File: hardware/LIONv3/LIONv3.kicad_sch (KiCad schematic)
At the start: 31 parts, among them SW1 RESET, SW2 BOOT, U14 HC-1_25-2PWT, U15 HC-1_25-2PWT, U19 HC-1_25-2PWT, U2 TYPE-C_16PIN_2MD(073), U21 USBLC6-2SC6, U3 ESP32-C6-MINI-1-N4, U4 TMP112AIDRLR, U9 HC-1_25-2PWT

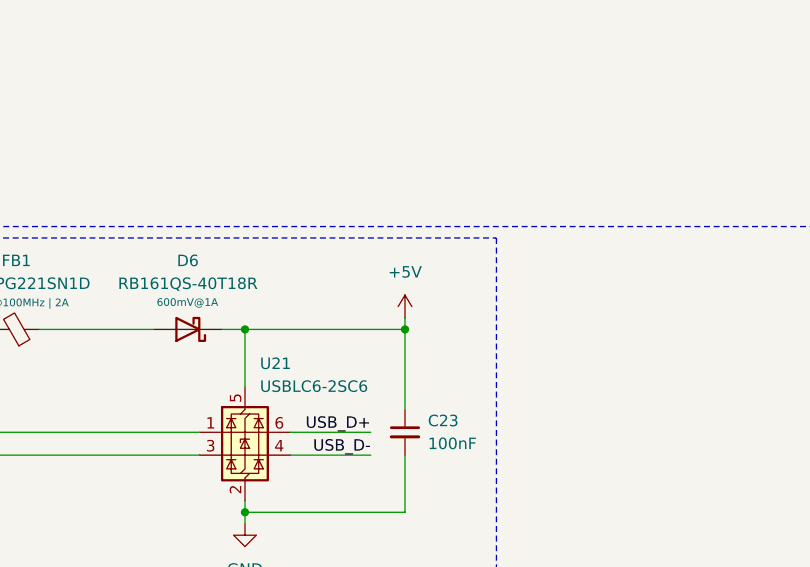
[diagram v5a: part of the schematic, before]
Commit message: refactor(hardware): rename power symbols
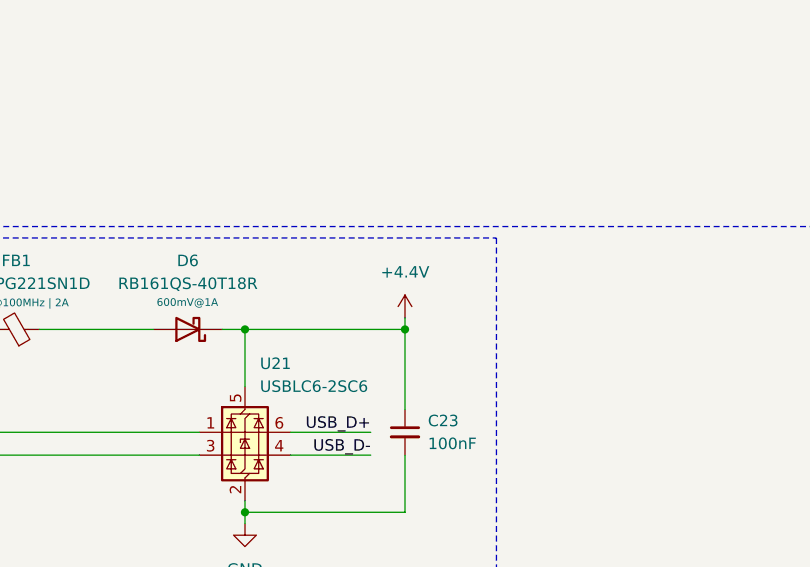
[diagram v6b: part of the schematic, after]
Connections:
- net +5V renamed +4.4V
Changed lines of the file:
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@@
+	)
+	(symbol
+		(lib_id "power:+5V")
+		(at 113.03 166.37 0)
+		(unit 1)
+		(body_style 1)
+		(exclude_from_sim no)
+		(in_bom yes)
+		(on_board yes)
+		(in_pos_files yes)
+		(dnp no)
+		(fields_autoplaced yes)
+		(property "Reference" "#PWR046"
+			(at 113.03 170.18 0)
+			(hide yes)
+			(show_name no)
+			(do_not_autoplace no)
+			(effects
+				(font
+					(size 1.27 1.27)
+				)
+			)
+		)
+		(property "Value" "+4.4V"
+			(at 113.03 161.29 0)
+			(show_name no)
+			(do_not_autoplace no)
+			(effects
+				(font
+					(size 1.27 1.27)
+				)
+			)
+		)
+		(property "Footprint" ""
+			(at 113.03 166.37 0)
+			(hide yes)
+			(show_name no)
+			(do_not_autoplace no)
+			(effects
+				(font
+					(size 1.27 1.27)
+				)
+			)
+		)
+		(property "Datasheet" ""
+			(at 113.03 166.37 0)
+			(hide yes)
+			(show_name no)
+			(do_not_autoplace no)
+			(effects
+				(font
+					(size 1.27 1.27)
+				)
+			)
+		)
+		(property "Description" "Power symbol creates a global label with name \"+5V\""
+			(at 113.03 166.37 0)
+			(hide yes)
+			(show_name no)
+			(do_not_autoplace no)
+			(effects
+				(font
+					(size 1.27 1.27)
+				)
+			)
+		)
+		(pin "1"
+		)
+		(instances
+			(project "LIONv3"
+				(path "/3cc9e06f-00d0-4bec-822f-2e156022ced4"
+					(reference "#PWR046")
+					(unit 1)
+				)
+			)
+		)
 	)
 	(symbol
@@
 					(unit 1)
 				)
-			)
-		)
-	)
-	(symbol
-		(lib_id "power:+5V")
-		(at 113.03 166.37 0)
-		(mirror y)
-		(unit 1)
-		(body_style 1)
-		(exclude_from_sim no)
-		(in_bom yes)
-		(on_board yes)
-		(in_pos_files yes)
-		(dnp no)
-		(fields_autoplaced yes)
-		(property "Reference" "#PWR02"
-			(at 113.03 170.18 0)
-			(hide yes)
-			(show_name no)
-			(do_not_autoplace no)
-			(effects
-				(font
-					(size 1.27 1.27)
-				)
-			)
-		)
-		(property "Value" "+5V"
-			(at 113.03 161.29 0)
-			(show_name no)
-			(do_not_autoplace no)
-			(effects
-				(font
-					(size 1.27 1.27)
-				)
-			)
-		)
-		(property "Footprint" ""
-			(at 113.03 166.37 0)
-			(hide yes)
-			(show_name no)
-			(do_not_autoplace no)
-			(effects
-				(font
-					(size 1.27 1.27)
-				)
-			)
-		)
-		(property "Datasheet" ""
-			(at 113.03 166.37 0)
-			(hide yes)
-			(show_name no)
-			(do_not_autoplace no)
-			(effects
-				(font
-					(size 1.27 1.27)
-				)
-			)
-		)
-		(property "Description" "Power symbol creates a global label with name \"+5V\""
-			(at 113.03 166.37 0)
-			(hide yes)
-			(show_name no)
-			(do_not_autoplace no)
-			(effects
-				(font
-					(size 1.27 1.27)
-				)
-			)
-		)
-		(pin "1"
-		)
-		(instances
-			(project "LIONv3"
-				(path "/3cc9e06f-00d0-4bec-822f-2e156022ced4"
-					(reference "#PWR02")
-					(unit 1)
-				)

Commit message: feat(hardware): major schematic improvements
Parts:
- C14, C15: value TBD -> DNP
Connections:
- net UART_RX0 renamed UART_RX
- net UART_TX0 renamed UART_TX
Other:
- moved on the sheet: D5, R7, R8, SW2

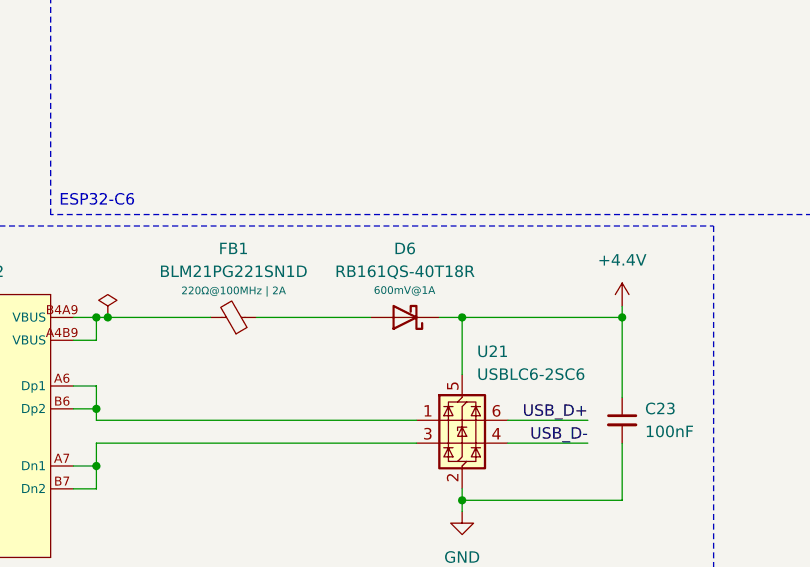
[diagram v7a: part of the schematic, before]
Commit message: feat(hardware): change schotkky diode to PMEG2010ER
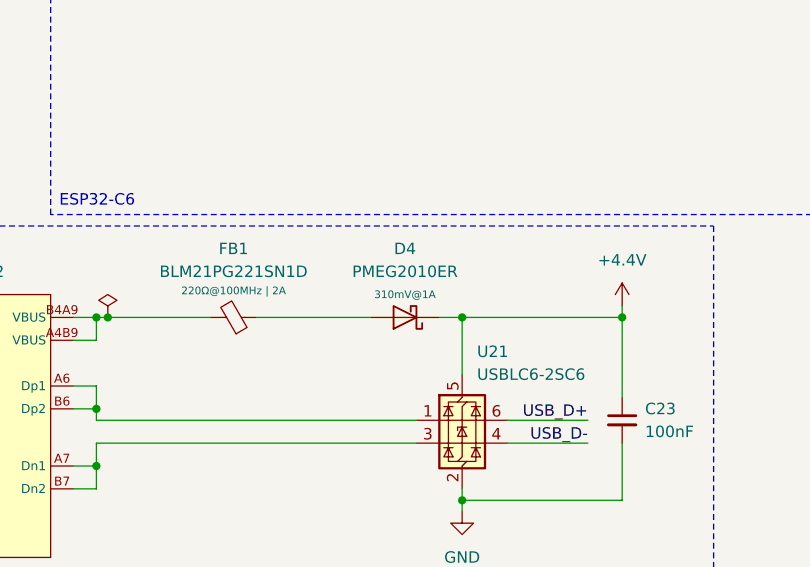
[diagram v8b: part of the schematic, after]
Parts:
- removed D6: RB161QS-40T18R, LIONv3-Footprints:X2-DFN1006-2_L1.0-W0.6-P0.65-RD, symbol Device:D_Schottky
- added D4: PMEG2010ER, Diode_SMD:Nexperia_CFP3_SOD-123W, symbol Diode:PMEG2010ER
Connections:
- net +4.4V: now also D4.1 (K)
- net at FB1.1: now also D4.2 (A)
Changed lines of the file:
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@@
+	)
+	(symbol
+		(lib_id "Diode:PMEG2010ER")
+		(at 88.9 167.64 180)
+		(unit 1)
+		(body_style 1)
+		(exclude_from_sim no)
+		(in_bom yes)
+		(on_board yes)
+		(in_pos_files yes)
+		(dnp no)
+		(property "Reference" "D4"
+			(at 88.9 160.02 0)
+			(show_name no)
+			(do_not_autoplace no)
+			(effects
+				(font
+					(size 1.27 1.27)
+				)
+			)
+		)
+		(property "Value" "PMEG2010ER"
+			(at 88.9 162.56 0)
+			(show_name no)
+			(do_not_autoplace no)
+			(effects
+				(font
+					(size 1.27 1.27)
+				)
+			)
+		)
+		(property "Footprint" "Diode_SMD:Nexperia_CFP3_SOD-123W"
+			(at 88.9 163.195 0)
+			(hide yes)
+			(show_name no)
+			(do_not_autoplace no)
+			(effects
+				(font
+					(size 1.27 1.27)
+				)
+			)
+		)
+		(property "Datasheet" "https://assets.nexperia.com/documents/data-sheet/PMEG2010ER.pdf"
+			(at 88.9 167.64 0)
+			(hide yes)
+			(show_name no)
+			(do_not_autoplace no)
+			(effects
+				(font
+					(size 1.27 1.27)
+				)
+			)
+		)
+		(property "Description" "20V, 1A low Vf MEGA Schottky barrier rectifier, SOD-123W"
+			(at 88.9 167.64 0)
+			(hide yes)
+			(show_name no)
+			(do_not_autoplace no)
+			(effects
+				(font
+					(size 1.27 1.27)
+				)
+			)
+		)
+		(property "Rating" "310mV@1A"
+			(at 88.9 165.1 0)
+			(show_name no)
+			(do_not_autoplace no)
+			(effects
+				(font
+					(size 0.8467 0.8467)
+				)
+			)
+		)
+		(property "LCSC" "C82288"
+			(at 88.9 167.64 0)
+			(hide yes)
+			(show_name no)
+			(do_not_autoplace no)
+			(effects
+				(font
+					(size 1.27 1.27)
+				)
+			)
+		)
+		(pin "2"
+		)
+		(pin "1"
+		)
+		(instances
+			(project "LIONv3"
+				(path "/3cc9e06f-00d0-4bec-822f-2e156022ced4"
+					(reference "D4")
+					(unit 1)
+				)
+			)
+		)
 	)
 	(symbol
@@
 					(unit 1)
 				)
-			)
-		)
-	)
-	(symbol
-		(lib_id "Device:D_Schottky")
-		(at 88.9 167.64 180)
-		(unit 1)
-		(body_style 1)
-		(exclude_from_sim no)
-		(in_bom yes)
-		(on_board yes)
-		(in_pos_files yes)
-		(dnp no)
-		(property "Reference" "D6"
-			(at 88.9 160.02 0)
-			(show_name no)
-			(do_not_autoplace no)
-			(effects
-				(font
-					(size 1.27 1.27)
-				)
-			)
-		)
-		(property "Value" "RB161QS-40T18R"
-			(at 88.9 162.56 0)
-			(show_name no)
-			(do_not_autoplace no)
-			(effects
-				(font
-					(size 1.27 1.27)
-				)
-			)
-		)
-		(property "Footprint" "LIONv3-Footprints:X2-DFN1006-2_L1.0-W0.6-P0.65-RD"
-			(at 88.9 167.64 0)
-			(hide yes)
-			(show_name no)
-			(do_not_autoplace no)
-			(effects
-				(font
-					(size 1.27 1.27)
-				)
-			)
-		)
-		(property "Datasheet" "https://www.lcsc.com/datasheet/C2837790.pdf"
-			(at 88.9 167.64 0)
-			(hide yes)
-			(show_name no)
-			(do_not_autoplace no)
-			(effects
-				(font
-					(size 1.27 1.27)
-				)
-			)
-		)
-		(property "Description" "Schottky diode"
-			(at 88.9 167.64 0)
-			(hide yes)
-			(show_name no)
-			(do_not_autoplace no)
-			(effects
-				(font
-					(size 1.27 1.27)
-				)
-			)
-		)
-		(property "LCSC" "C2837790"
-			(at 88.9 167.64 0)
-			(hide yes)
-			(show_name no)
-			(do_not_autoplace no)
-			(effects
-				(font
-					(size 1.27 1.27)
-				)
-			)
-		)
-		(property "Rating" "600mV@1A"
-			(at 88.8522 164.6334 0)
-			(show_name no)
-			(do_not_autoplace no)
-			(effects
-				(font
-					(size 0.8467 0.8467)
-				)
-			)
-		)
-		(pin "2"
-		)
-		(pin "1"
-		)
-		(instances
-			(project "LIONv3"
-				(path "/3cc9e06f-00d0-4bec-822f-2e156022ced4"
-					(reference "D6")
-					(unit 1)
-				)
